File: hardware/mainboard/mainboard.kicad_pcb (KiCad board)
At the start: 4 copper layers, 101.8 x 66.2 mm, 83 parts, among them J1 USB_C_Receptacle_USB2.0_16P, J2 Conn_01x03_Pin, J3 Barrel_Jack_MountingPin, J4 Conn_01x04_Socket, J5 Conn_01x04_Socket, J6 Screw_Terminal_01x02, J7 Conn_01x02_Socket, J8 Conn_01x02_Socket, J9 Conn_01x04_Socket, Q1 BTN8982TA, Q2 AO3400A, Q3 AO3400A, Q6 BTN8982TA, U1 ESP32-S3-WROOM-1, U2 USBLC6-2SC6, U3 AP2112K-3.3, U4 TPS2116DRL, U5 TPS62161DSG

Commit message: finished component placement
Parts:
- removed the C14 at (29.9, 54.5)
- J9: footprint Connector_PinHeader_2.54mm:PinHeader_1x04_P2.54mm_Vertical -> Connector_PinSocket_2.54mm:PinSocket_1x04_P2.54mm_Vertical
- moved R1 198.5 mm to (228.0, 76.3), turned to -90 degrees
- moved R2 193.2 mm to (219.2, 104.3), turned to -90 degrees
- moved C13 149.6 mm to (173.6, 93.5), turned to -90 degrees
- moved C9 148.8 mm to (172.2, 89.3), turned to 90 degrees
- moved R7 148.1 mm to (176.5, 97.2)
- moved R8 147.8 mm to (176.4, 98.7), turned to 180 degrees
- moved C8 147.3 mm to (172.2, 77.1), turned to 90 degrees
- moved R9 146.1 mm to (178.3, 84.3)
- moved R10 146.0 mm to (178.3, 85.9)
- moved +5V_USB 138.6 mm to (229.6, 66.1)
- moved C17 137.6 mm to (176.8, 90.5), turned to 90 degrees
- moved R11 134.2 mm to (175.3, 93.5), turned to -90 degrees
- moved C18 133.9 mm to (176.8, 78.3), turned to 90 degrees
- moved C14 132.6 mm to (173.6, 81.4), turned to -90 degrees
- moved C12 132.0 mm to (152.0, 99.6), turned to -90 degrees
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- renumbered TP3 to +12V, TP6 to +3V3, TP5 to +5V, TP4 to +5V_USB, TP8 to PWM3, TP7 to PWM4, TP2 to RX, TP1 to TX
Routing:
- net /VBUS_1: track 5.02 -> 7.56 mm
- net /5V_SEL: track 11.1 -> 9.37 mm
- added copper zone on F.Cu, net /FAN_GND

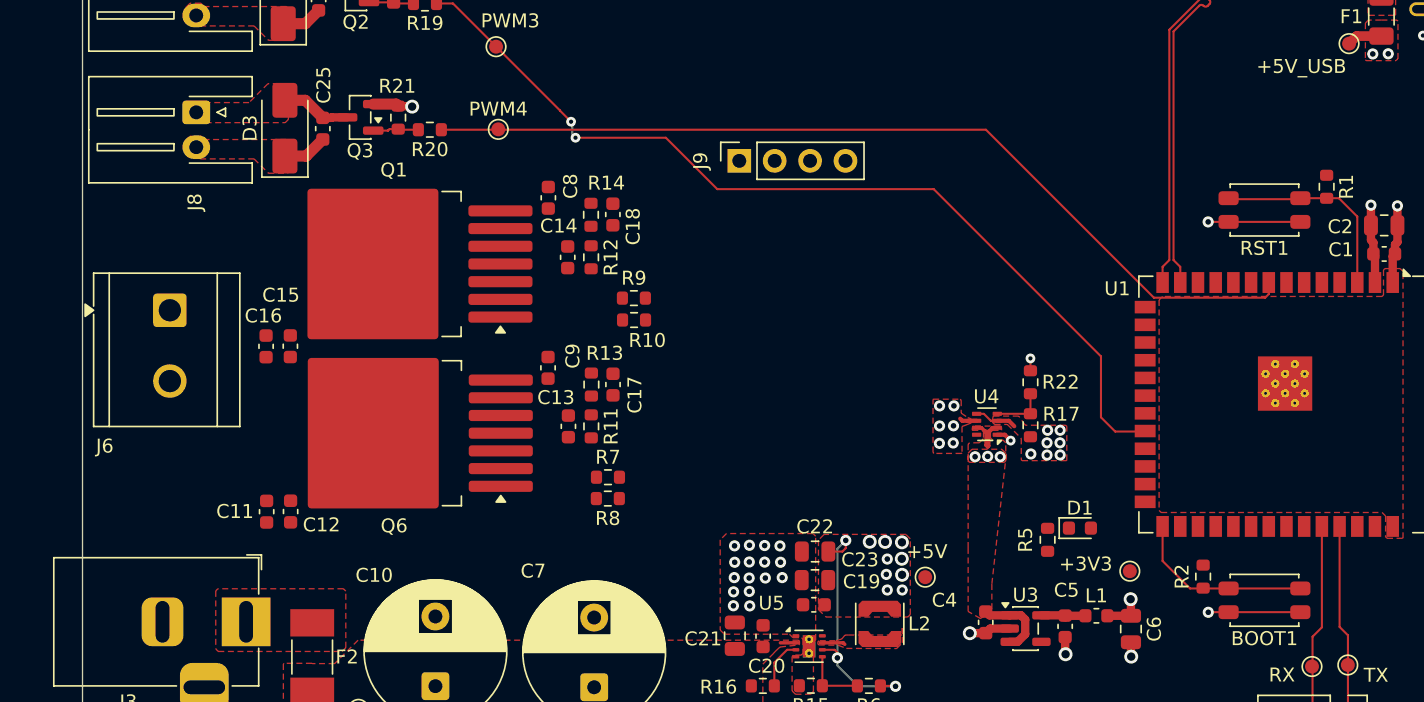
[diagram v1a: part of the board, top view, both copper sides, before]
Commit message: finished h-bridge power routing
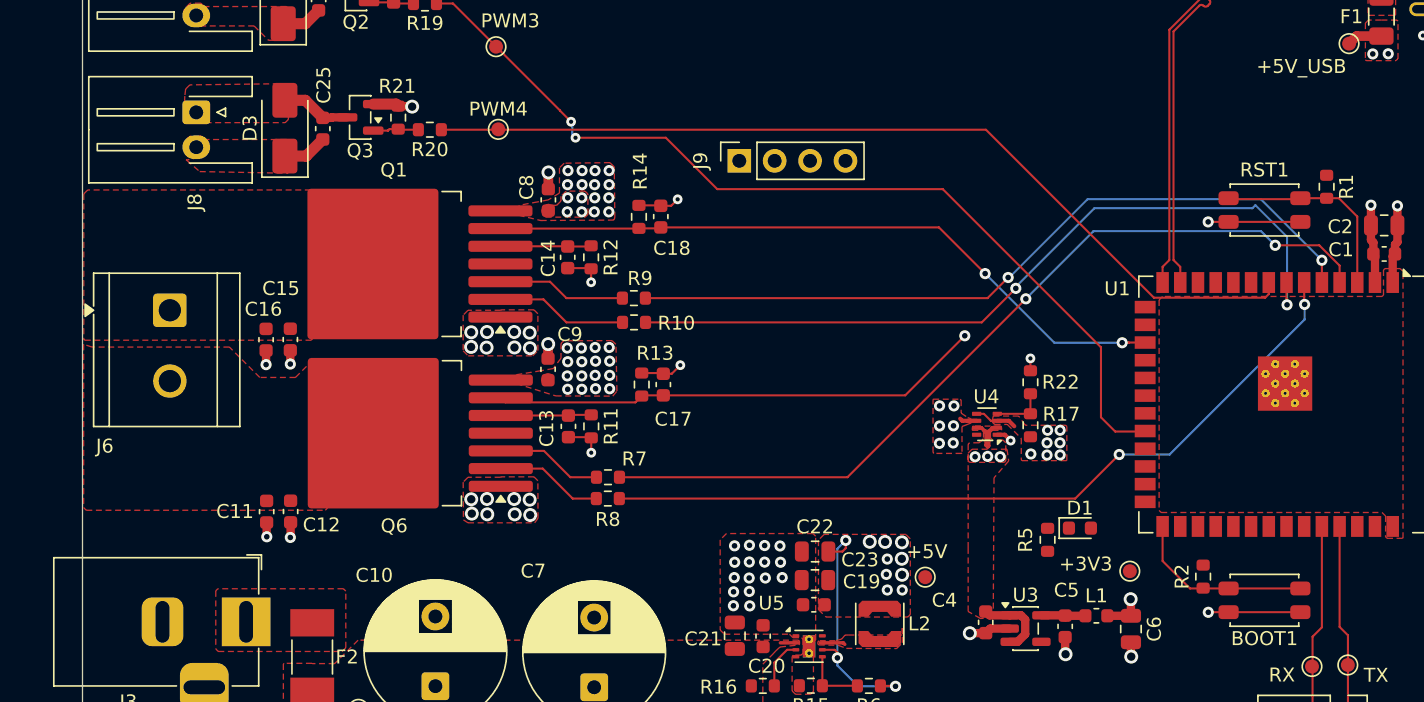
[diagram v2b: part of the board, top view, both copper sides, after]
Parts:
- moved C17 3.61 mm to (180.4, 90.5)
- moved R13 3.61 mm to (178.9, 90.5)
- moved C18 3.44 mm to (180.2, 78.5)
- moved R14 3.44 mm to (178.7, 78.5)
- moved C16 0.48 mm to (151.9, 87.3)
- moved C15 0.48 mm to (153.7, 87.3)
- moved R10 0.17 mm to (178.3, 86.1), turned to 180 degrees
- moved C8 0.15 mm to (172.2, 77.3)
- moved C9 0.11 mm to (172.2, 89.4)
- turned R7 to 180 degrees
- turned R9 to 180 degrees
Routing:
- net INH_1: track 0.00 -> 61.2 mm, vias 0 -> 2
- net PELT_H1: track 0.00 -> 57.2 mm, vias 0 -> 2
- net PELT_H2: track 0.00 -> 57.0 mm, vias 0 -> 2
- net INH_2: track 0.00 -> 54.9 mm, vias 0 -> 2
- net IS_2: track 0.00 -> 49.7 mm, vias 0 -> 2
- net IS_1: track 0.00 -> 35.4 mm, vias 0 -> 1
- net GND: track 36.2 -> 51.9 mm, vias 30 -> 54
- net /IN2: track 0.00 -> 9.44 mm
- net /INH2: track 0.00 -> 9.24 mm
- net /IN: track 0.00 -> 7.75 mm
- net /INH: track 0.00 -> 7.65 mm
- net /SR2: track 0.00 -> 6.53 mm
- net /SR: track 0.00 -> 6.51 mm
- net +12V: track 7.26 -> 9.72 mm, vias 0 -> 34
- added copper zone on In2.Cu, net +12V
- added copper zone on F.Cu, net /PELT+
- added copper zone on F.Cu, net /PELT-
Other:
- board text added: "100nF"

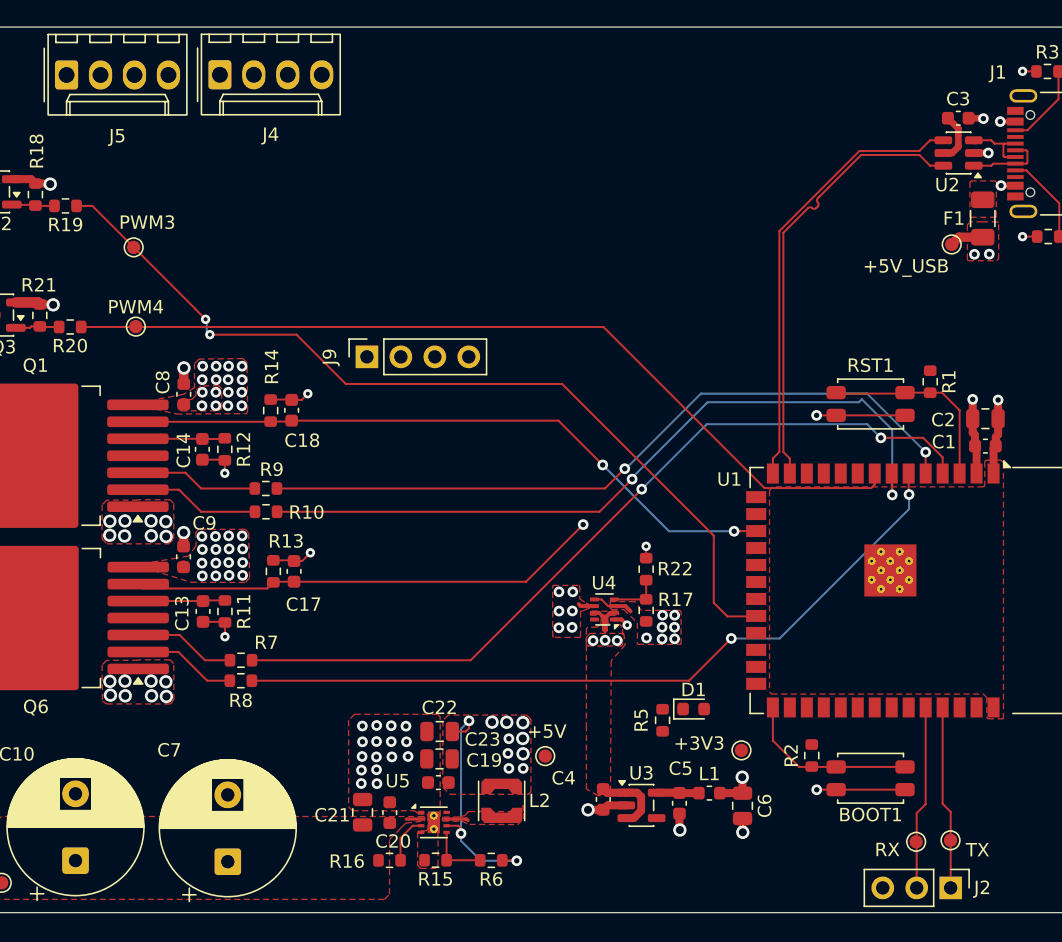
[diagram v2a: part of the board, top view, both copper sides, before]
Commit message: signal routing for pwm fans and h-bridge
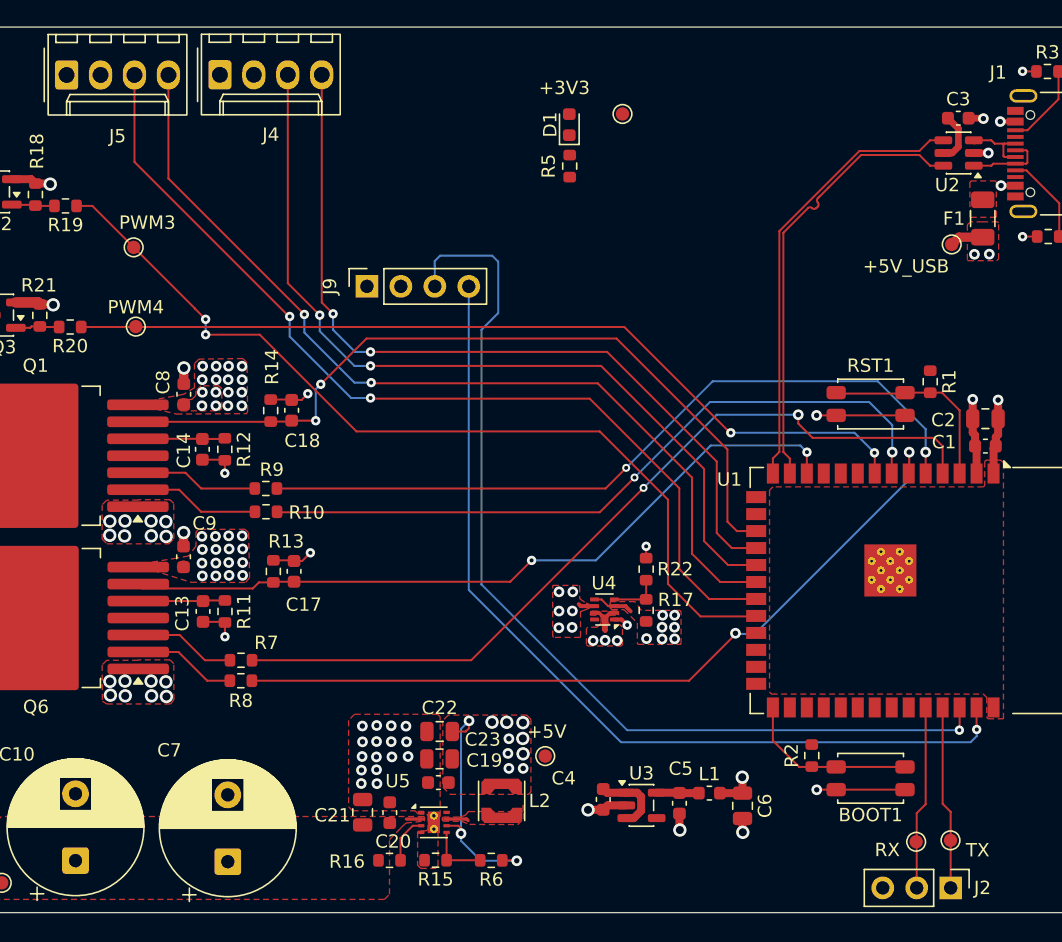
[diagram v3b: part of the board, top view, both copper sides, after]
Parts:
- moved +3V3 48.4 mm to (205.0, 56.3)
- moved D1 44.7 mm to (201.0, 57.1), turned to 90 degrees
- moved R5 42.0 mm to (201.1, 60.2)
- moved J9 5.27 mm to (185.9, 69.2)
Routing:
- net SCL: track 0.00 -> 73.6 mm, vias 0 -> 1
- net TACH2: track 0.00 -> 71.0 mm, vias 0 -> 2
- net PWM2: track 0.00 -> 68.3 mm, vias 0 -> 2
- net SDA: track 0.00 -> 67.8 mm, vias 0 -> 1
- net TACH1: track 0.00 -> 63.2 mm, vias 0 -> 2
- net PWM1: track 0.00 -> 61.1 mm, vias 0 -> 2
- net IS_1: track 35.4 -> 56.4 mm, vias 1 -> 2
- net IS_2: track 49.7 -> 59.3 mm
- net PELT_H2: track 57.0 -> 53.8 mm
- net PELT_H1: track 57.2 -> 59.2 mm
- net INH_2: track 54.9 -> 56.7 mm
- net INH_1: track 61.2 -> 62.7 mm
- net PWM3: track 67.0 -> 68.0 mm
- net +5V: track 22.2 -> 21.6 mm
- net PWM4: track 65.3 -> 64.8 mm, vias 0 -> 2
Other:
- board text added: "+3V3"

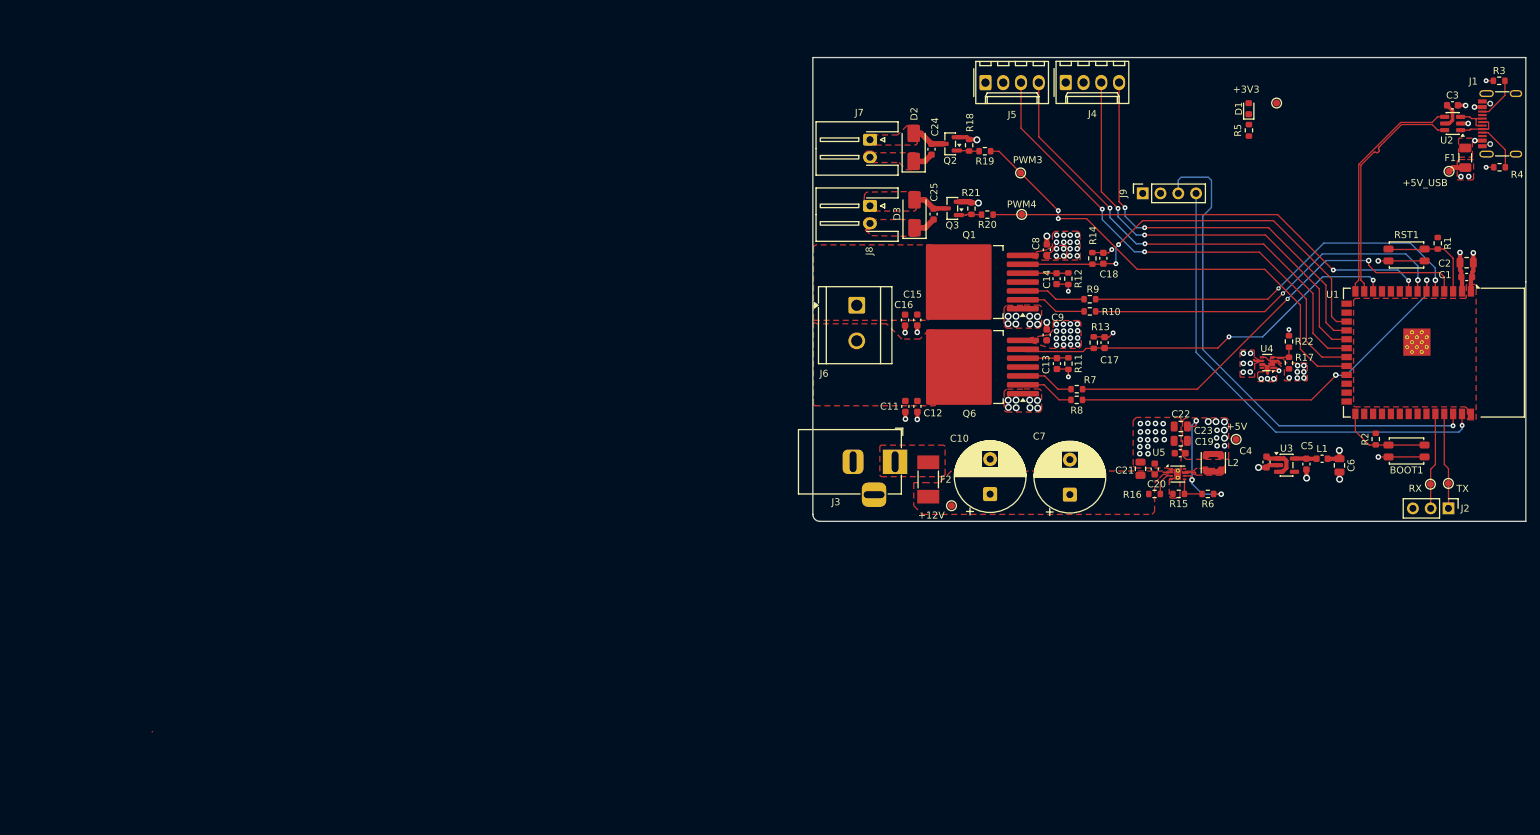
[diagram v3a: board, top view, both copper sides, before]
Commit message: revised routing and power stage routing
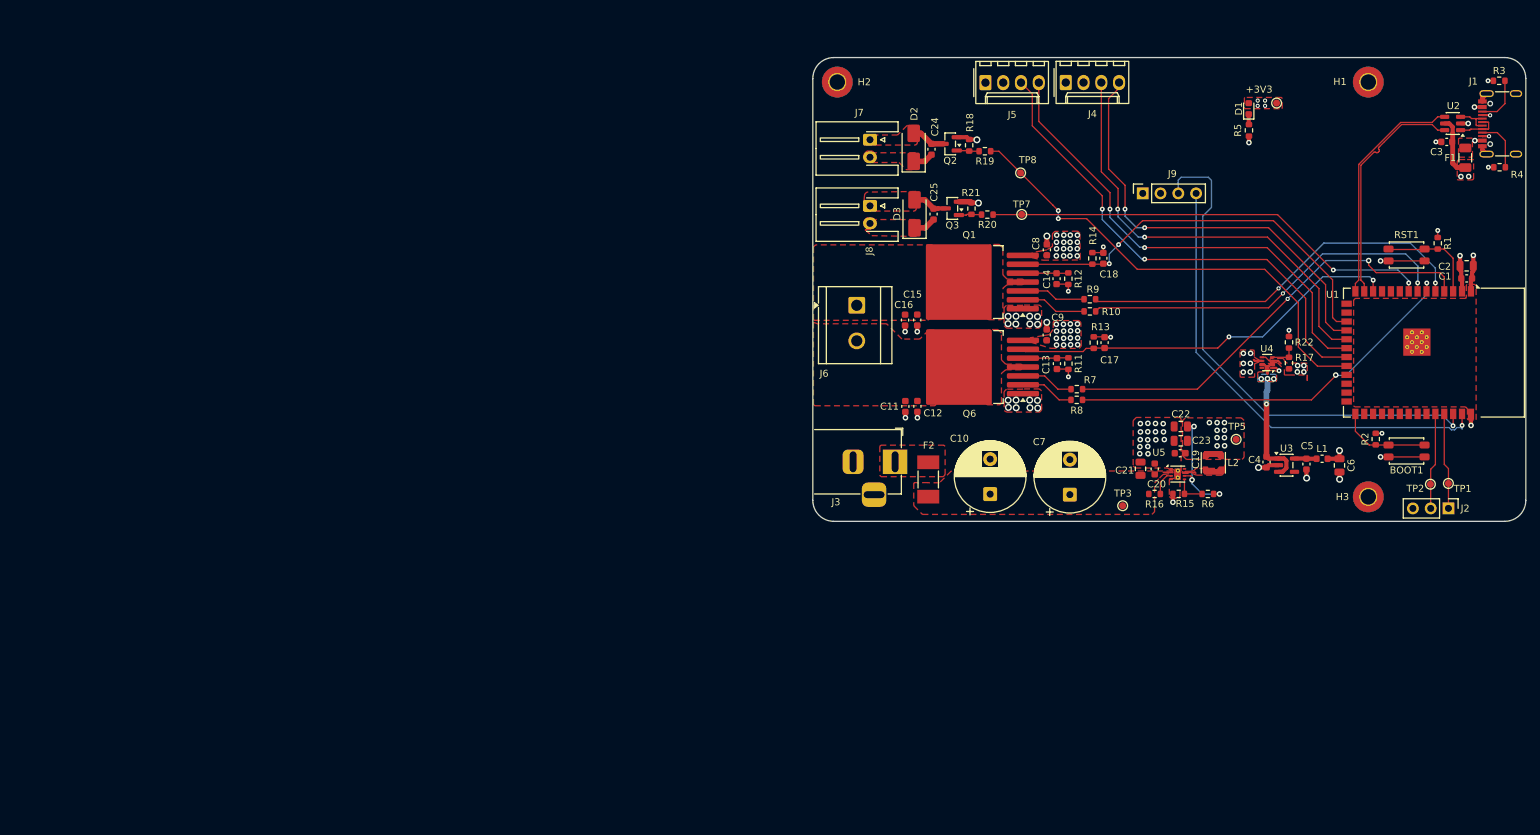
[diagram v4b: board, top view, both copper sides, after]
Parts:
- removed +5V_USB: TestPoint_VBUS, TestPoint:TestPoint_Pad_D1.0mm
- added H1: MountingHole_Pad, MountingHole:MountingHole_2.2mm_M2_Pad_TopBottom, F.Cu at (218.1, 53.3)
- added H2: MountingHole_Pad, MountingHole:MountingHole_2.2mm_M2_Pad_TopBottom, F.Cu at (142.2, 53.3)
- added H3: MountingHole_Pad, MountingHole:MountingHole_2.2mm_M2_Pad_TopBottom, F.Cu at (218.1, 112.5)
- moved TP3 24.4 mm to (183.0, 113.8)
- moved C3 5.29 mm to (229.3, 61.9), turned to 180 degrees
- moved C2 0.45 mm to (232.2, 79.5)
- moved C1 0.20 mm to (232.2, 81.3)
- moved R22 0.12 mm to (206.8, 90.5)
- renumbered TX to TP1, RX to TP2, +12V to TP3, +5V to TP5, +3V3 to TP6, PWM4 to TP7, PWM3 to TP8
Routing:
- net /5V_SEL: track 9.37 -> 20.6 mm, vias 3 -> 4
- net GND: track 51.9 -> 57.0 mm, vias 54 -> 59
- net +5V: track 21.6 -> 19.2 mm, vias 19 -> 16
- net /VBUS_1: track 7.56 -> 9.84 mm
- net Net-(D1-K): track 0.00 -> 1.50 mm
- net +3V3: track 8.56 -> 9.98 mm, vias 2 -> 8
- net PWM1: track 61.1 -> 62.2 mm
- net PELT_H1: track 59.2 -> 58.4 mm
- net /CC1: track 6.79 -> 7.56 mm
- net /CC2: track 6.26 -> 6.96 mm
- net IS_2: track 59.3 -> 58.8 mm
- added copper zone on F.Cu, net +3V3
- added copper zone on In2.Cu, net +3V3
- added copper zone on In2.Cu, net +5V
- added copper zone on B.Cu, net /5V_SEL
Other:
- board size 101.8 x 66.2 mm -> 101.9 x 66.3 mm
